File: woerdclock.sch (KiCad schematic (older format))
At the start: 88 parts, among them K1 Sound, K10 WS2812B_OUT, K11 WS2812B_IN, K12 WS2812B_IN, K13 WS2812B_OUT, K14 WS2812B_OUT, K15 WS2812B_IN, K16 WS2812B_IN, K17 WS2812B_OUT, K18 WS2812B_OUT, K19 WS2812B_IN, K2 IR, K20 WS2812B_IN, K21 WS2812B_OUT, K22 WS2812B_OUT, K23 WS2812B_IN, K24 WS2812B_IN, K25 WS2812B_OUT, K26 WS2812B_OUT, K27 WS2812B_IN, K3 3V3, K4 WS2812B_OUT, K5 WS2812B_OUT, K6 WS2812B_IN, K7 WS2812B_IN, K8 WS2812B_IN, K9 WS2812B_OUT, P10 CONN_1, P11 CONN_3X2, P12 CONN_1, P13 CONN_1, P14 CONN_1, P15 CONN_1, P16 CONN_1, P17 CONN_1, P4 CONN_1, P5 CONN_1, P6 CONN_1, P7 CONN_1, P8 CONN_3X2, P9 CONN_1, SW1 up, SW2 ok, SW3 down, U1 RFM12B, U10 DCF77, U11 DHT, U14 SD-CARD, U2 RTC_MODUL, U3 ARDUINO_PRO_MICRO, U4 BH1750FVI_MODULE, U5 5V 8A -Co+, U8 ESP8266, U9 10DOF

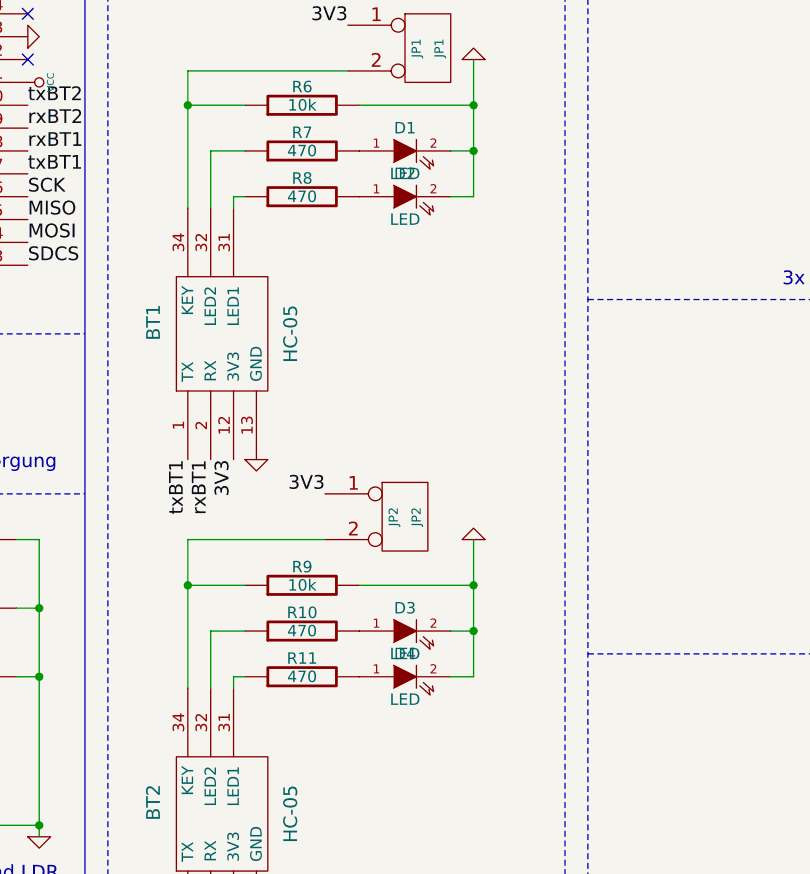
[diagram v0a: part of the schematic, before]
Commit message: Fottprint of Bluetooth Modules where to wide - fixed.
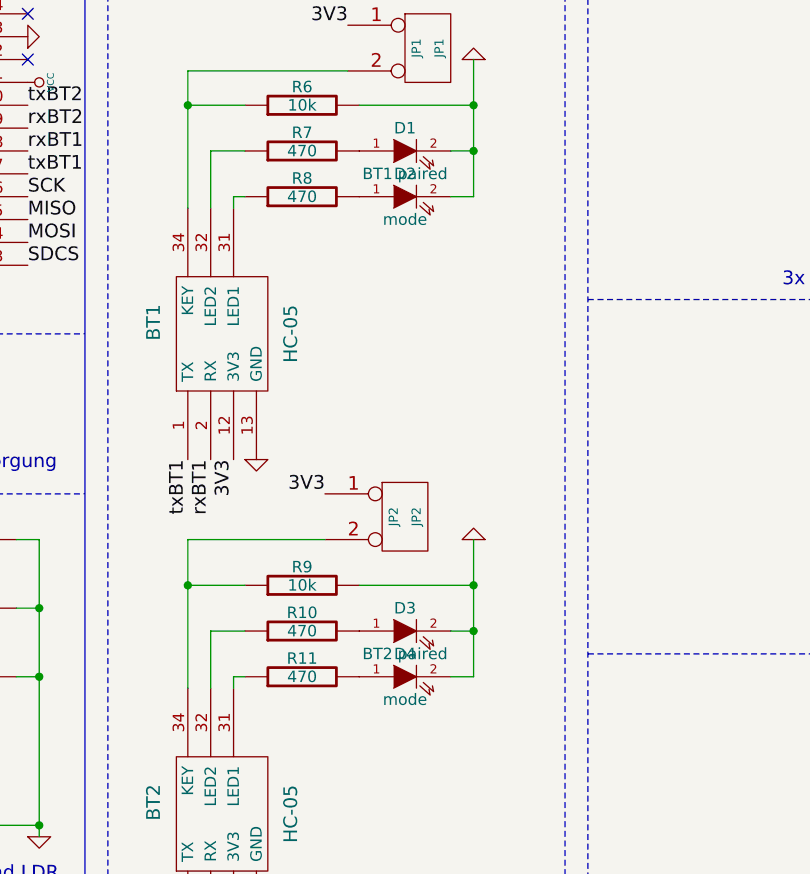
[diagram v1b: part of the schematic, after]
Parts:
- D1: value LED -> BT1 paired
- D2, D4: value LED -> mode
- D3: value LED -> BT2 paired
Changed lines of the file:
@@
 P 4400 1450
 F 0 "D1" H 4400 1550 50  0000 C CNN
-F 1 "LED" H 4400 1350 50  0000 C CNN
+F 1 "BT1 paired" H 4400 1350 50  0000 C CNN
 F 2 "" H 4400 1450 60  0001 C CNN
 F 3 "" H 4400 1450 60  0001 C CNN
@@
 P 4400 1650
 F 0 "D2" H 4400 1750 50  0000 C CNN
-F 1 "LED" H 4400 1550 50  0000 C CNN
+F 1 "mode" H 4400 1550 50  0000 C CNN
 F 2 "" H 4400 1650 60  0001 C CNN
 F 3 "" H 4400 1650 60  0001 C CNN
@@
 P 4400 3750
 F 0 "D4" H 4400 3850 50  0000 C CNN
-F 1 "LED" H 4400 3650 50  0000 C CNN
+F 1 "mode" H 4400 3650 50  0000 C CNN
 F 2 "" H 4400 3750 60  0001 C CNN
 F 3 "" H 4400 3750 60  0001 C CNN
@@
 P 4400 3550
 F 0 "D3" H 4400 3650 50  0000 C CNN
-F 1 "LED" H 4400 3450 50  0000 C CNN
+F 1 "BT2 paired" H 4400 3450 50  0000 C CNN
 F 2 "" H 4400 3550 60  0001 C CNN
 F 3 "" H 4400 3550 60  0001 C CNN
